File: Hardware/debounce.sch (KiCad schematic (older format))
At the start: 16 parts, among them U2 SN74AHC14RGYR

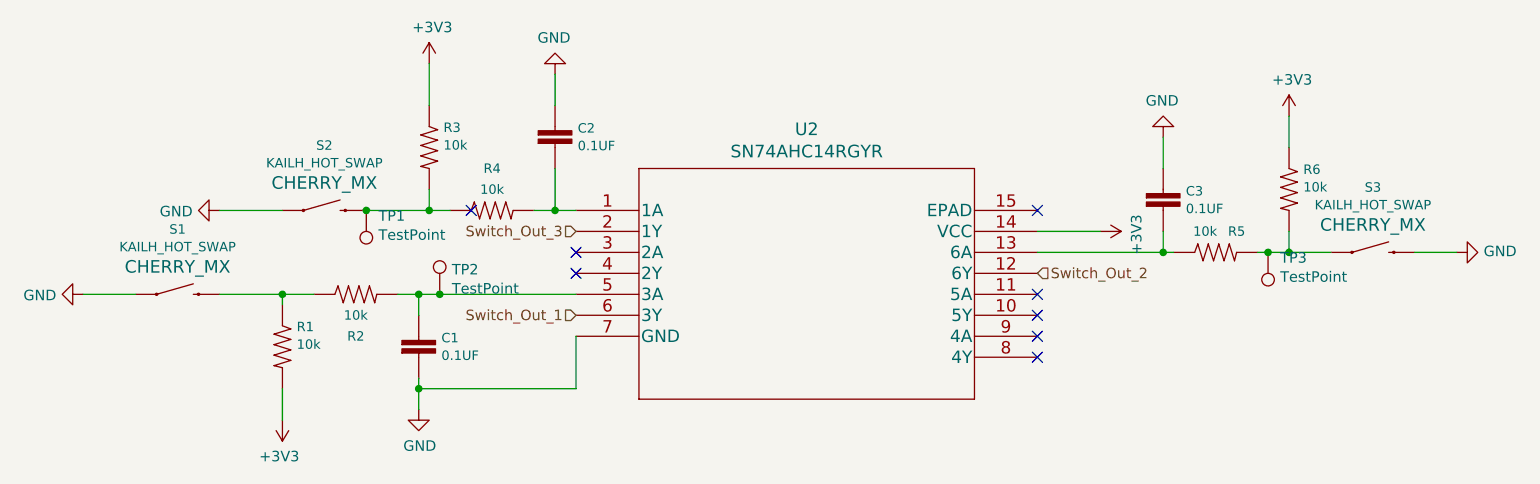
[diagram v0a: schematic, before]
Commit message: Complete new schematic
Added MAX232 and fixed test points on switches
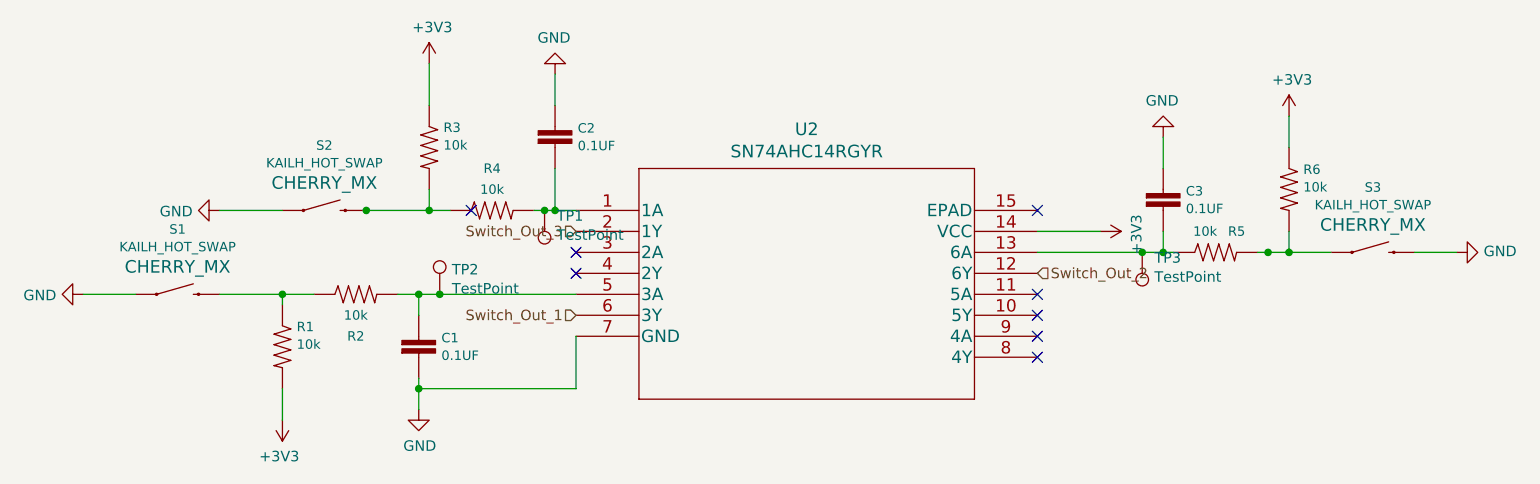
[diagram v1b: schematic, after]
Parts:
- TP1, TP2: footprint TestPoint:TestPoint_Pad_1.0x1.0mm -> TestPoint:TestPoint_THTPad_1.0x1.0mm_Drill0.5mm
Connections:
- net at C2.2, R4.2, U2.1 (1A): now also TP1.1
- net at R3.2, R4.1, S2.2: no longer TP1.1
- net at C3.2, R5.1, U2.13 (6A): now also TP3.1
- net at R5.2, R6.2, S3.1: no longer TP3.1
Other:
- moved on the sheet: TP1, TP3
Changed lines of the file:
@@
 	4650 3550 4650 3750
 Wire Wire Line
-	4550 3750 4650 3750
+	4550 3750 4600 3750
 Connection ~ 4650 3750
 Wire Wire Line
@@
 $EndComp
 Wire Wire Line
-	6950 3950 7550 3950
+	6950 3950 7450 3950
 Wire Wire Line
 	6950 3850 7250 3850
@@
 L Connector:TestPoint TP?
 U 1 1 5F4E2371
-P 3750 3750
+P 4600 3750
 AR Path="/5F4E2371" Ref="TP?"  Part="1"
 AR Path="/5F413993/5F4E2371" Ref="TP1"  Part="1"
-F 0 "TP1" H 3692 3776 50  0000 R CNN
-F 1 "TestPoint" H 3692 3867 50  0000 R CNN
-F 2 "TestPoint:TestPoint_Pad_1.0x1.0mm" H 3950 3750 50  0001 C CNN
-F 3 "~" H 3950 3750 50  0001 C CNN
-	1    3750 3750
+F 0 "TP1" H 4542 3776 50  0000 R CNN
+F 1 "TestPoint" H 4542 3867 50  0000 R CNN
+F 2 "TestPoint:TestPoint_THTPad_1.0x1.0mm_Drill0.5mm" H 4800 3750 50  0001 C CNN
+F 3 "~" H 4800 3750 50  0001 C CNN
+	1    4600 3750
 	-1   0    0    1
 $EndComp
@@
 F 0 "TP2" H 4158 4268 50  0000 L CNN
 F 1 "TestPoint" H 4158 4177 50  0000 L CNN
-F 2 "TestPoint:TestPoint_Pad_1.0x1.0mm" H 4300 4150 50  0001 C CNN
+F 2 "TestPoint:TestPoint_THTPad_1.0x1.0mm_Drill0.5mm" H 4300 4150 50  0001 C CNN
 F 3 "~" H 4300 4150 50  0001 C CNN
 	1    4100 4150
@@
 L Connector:TestPoint TP?
 U 1 1 5F4E2380
-P 8050 3950
+P 7450 3950
 AR Path="/5F4E2380" Ref="TP?"  Part="1"
 AR Path="/5F413993/5F4E2380" Ref="TP3"  Part="1"
-F 0 "TP3" H 7992 3976 50  0000 R CNN
-F 1 "TestPoint" H 7992 4067 50  0000 R CNN
-F 2 "TestPoint:TestPoint_THTPad_1.0x1.0mm_Drill0.5mm" H 8250 3950 50  0001 C CNN
-F 3 "~" H 8250 3950 50  0001 C CNN
-	1    8050 3950
+F 0 "TP3" H 7392 3976 50  0000 R CNN
+F 1 "TestPoint" H 7392 4067 50  0000 R CNN
+F 2 "TestPoint:TestPoint_THTPad_1.0x1.0mm_Drill0.5mm" H 7650 3950 50  0001 C CNN
+F 3 "~" H 7650 3950 50  0001 C CNN
+	1    7450 3950
 	-1   0    0    1
 $EndComp
@@
 	0    -1   -1   0
 $EndComp
+Connection ~ 4600 3750
+Wire Wire Line
+	4600 3750 4650 3750
+Connection ~ 7450 3950
+Wire Wire Line
+	7450 3950 7550 3950
 $EndSCHEMATC

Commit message: Add more net labels
Begin redesigning PCB again
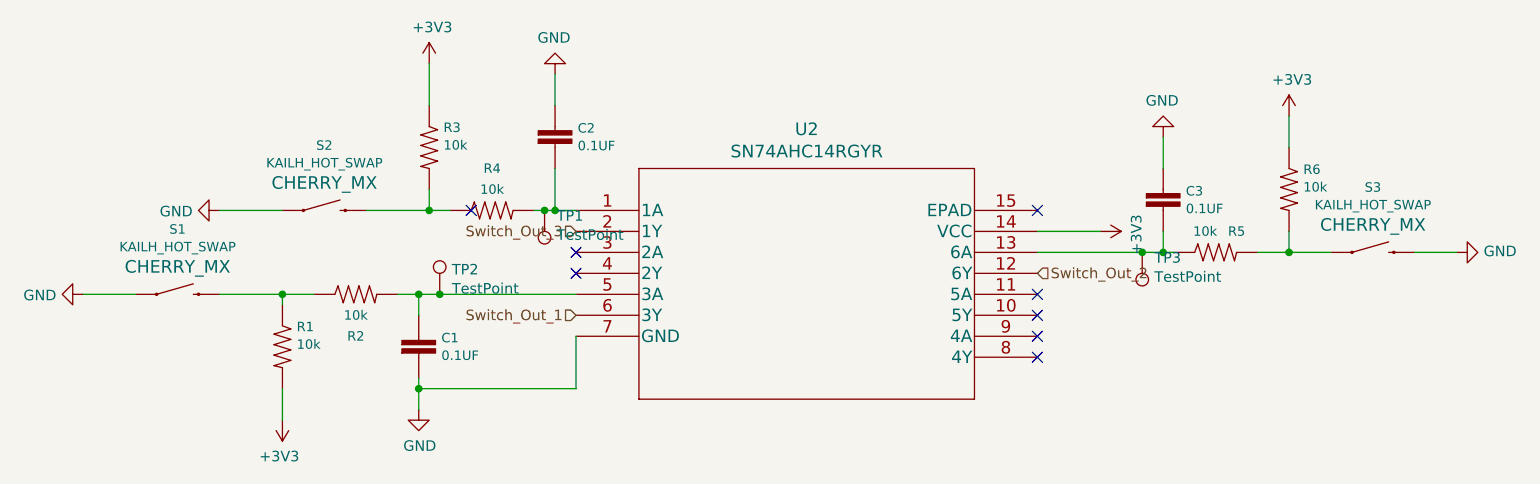
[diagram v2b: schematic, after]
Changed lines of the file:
@@
 	8150 3850 8150 3950
-Wire Wire Line
-	8000 3950 8050 3950
 Wire Wire Line
 	7550 3950 7600 3950
@@
 	-1   0    0    1
 $EndComp
-Connection ~ 3750 3750
 $Comp
 L Connector:TestPoint TP?
@@
 	-1   0    0    1
 $EndComp
-Connection ~ 8050 3950
-Wire Wire Line
-	8050 3950 8150 3950
 Wire Wire Line
 	8750 3950 8950 3950
@@
 Wire Wire Line
 	7450 3950 7550 3950
+Wire Wire Line
+	8000 3950 8150 3950
 $EndSCHEMATC

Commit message: Fix faulty debounce circuit
Used wrong value resistor/misplaced on each switch.
Also adjusted value of RC circuits for a time constant of 1 microsecond (was 1 millisecond before)
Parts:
- C1, C2, C3: value 0.1UF -> 10nF
- R2, R4, R5: value 10k -> 1k
- TP1, TP2, TP3: footprint TestPoint:TestPoint_THTPad_1.0x1.0mm_Drill0.5mm -> TestPoint:TestPoint_Pad_1.0x1.0mm
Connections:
- net at R2.1, S1.2: no longer R1.1
- net at C1.1, R2.2, TP2.1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: now also R1.1
- net at C2.2, R4.2, TP1.1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: now also R3.2
- net at R4.1, S2.2: no longer R3.2
- net at C3.2, R5.1, TP3.1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: now also R6.2
- net at R5.2, S3.1: no longer R6.2
- no-connect marks 8 -> 7
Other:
- moved on the sheet: R2, R3, R4, R5, R6, S2
